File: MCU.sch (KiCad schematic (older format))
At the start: 17 parts

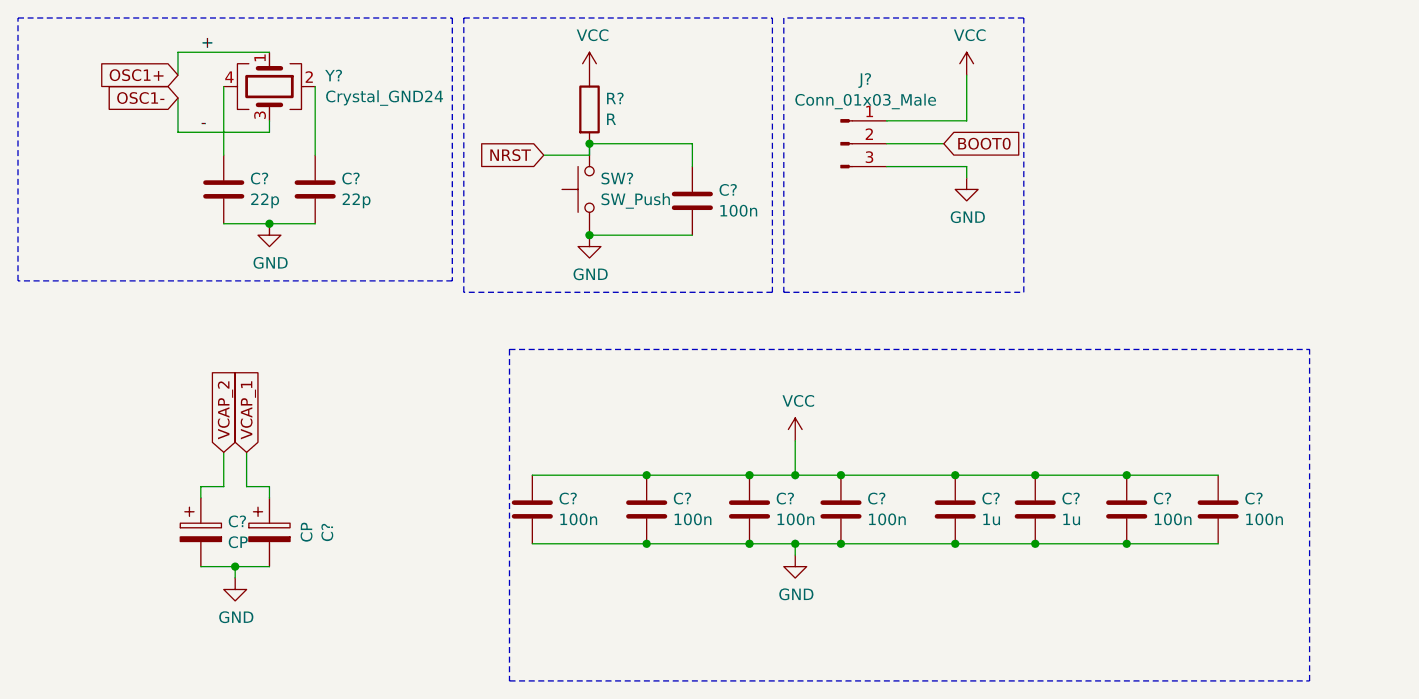
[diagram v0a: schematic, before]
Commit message: 4 layer add
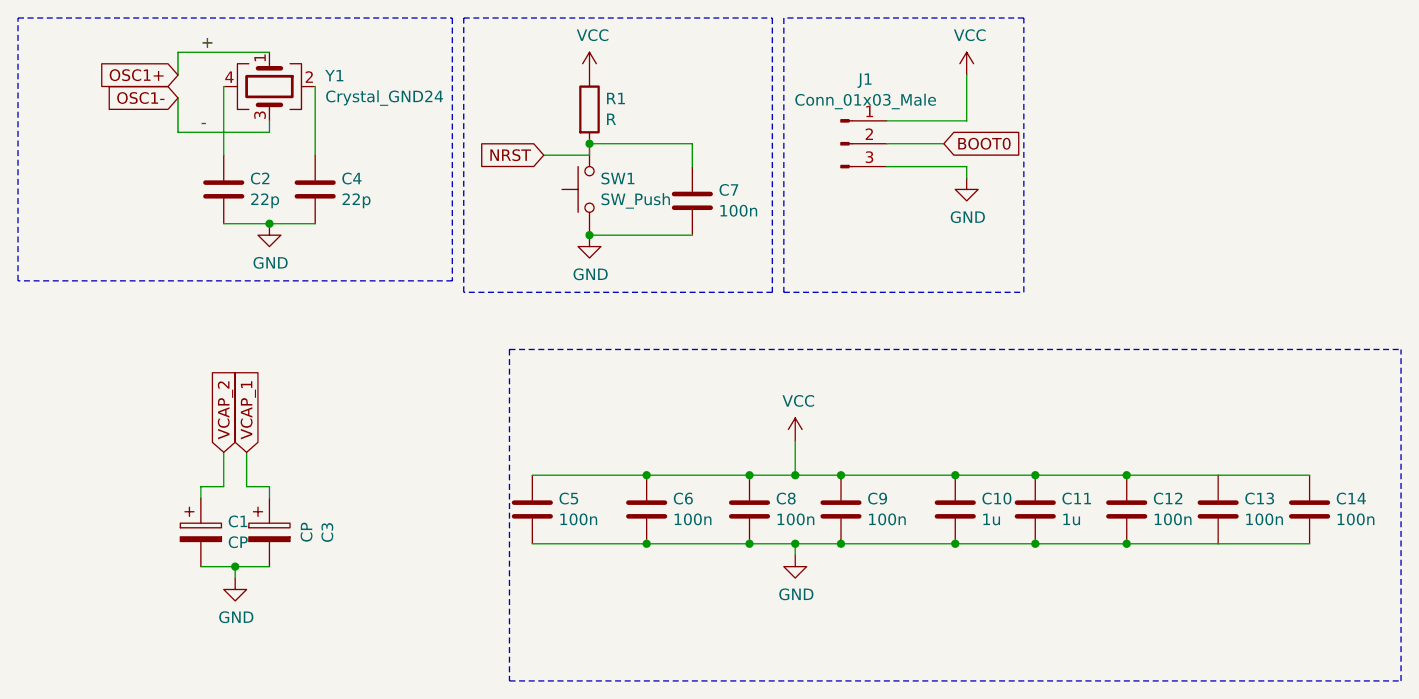
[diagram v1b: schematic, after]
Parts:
- added C14: 100n, Capacitor_SMD:C_0402_1005Metric, symbol Device:C
- gave numbers to parts that had none: 17
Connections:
- net GND: now also C14.2
- net VCC: now also C14.1

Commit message: a
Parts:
- C1: footprint Capacitor_SMD:C_1206_3216Metric -> Capacitor_SMD:C_0805_2012Metric_Pad1.15x1.40mm_HandSolder
- C3: footprint Capacitor_SMD:C_1206_3216Metric -> Capacitor_SMD:C_0805_2012Metric
- J1: footprint Connector_PinHeader_2.54mm:PinHeader_1x03_P2.54mm_Vertical -> Connector_PinHeader_2.54mm:PinHeader_1x03_P2.54mm_Vertical_SMD_Pin1Left
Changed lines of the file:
@@
 F 0 "J1" H 6958 3181 50  0000 C CNN
 F 1 "Conn_01x03_Male" H 6958 3090 50  0000 C CNN
-F 2 "Connector_PinHeader_2.54mm:PinHeader_1x03_P2.54mm_Vertical" H 6850 2900 50  0001 C CNN
+F 2 "Connector_PinHeader_2.54mm:PinHeader_1x03_P2.54mm_Vertical_SMD_Pin1Left" H 6850 2900 50  0001 C CNN
 F 3 "~" H 6850 2900 50  0001 C CNN
 	1    6850 2900
@@
 F 0 "C3" V 4605 4600 50  0000 C CNN
 F 1 "CP" V 4514 4600 50  0000 C CNN
-F 2 "Capacitor_SMD:C_1206_3216Metric" H 4388 4450 50  0001 C CNN
+F 2 "Capacitor_SMD:C_0805_2012Metric" H 4388 4450 50  0001 C CNN
 F 3 "~" H 4350 4600 50  0001 C CNN
 	1    4350 4600
@@
 F 0 "C1" H 4168 4646 50  0000 L CNN
 F 1 "CP" H 4168 4555 50  0000 L CNN
-F 2 "Capacitor_SMD:C_1206_3216Metric" H 4088 4450 50  0001 C CNN
+F 2 "Capacitor_SMD:C_0805_2012Metric_Pad1.15x1.40mm_HandSolder" H 4088 4450 50  0001 C CNN
 F 3 "~" H 4050 4600 50  0001 C CNN
 	1    4050 4600
